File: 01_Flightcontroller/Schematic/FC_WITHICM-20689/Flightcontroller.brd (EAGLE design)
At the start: 63.5 x 63.2 mm, 101 parts, among them Y1 8MHz, Y2 16MHz

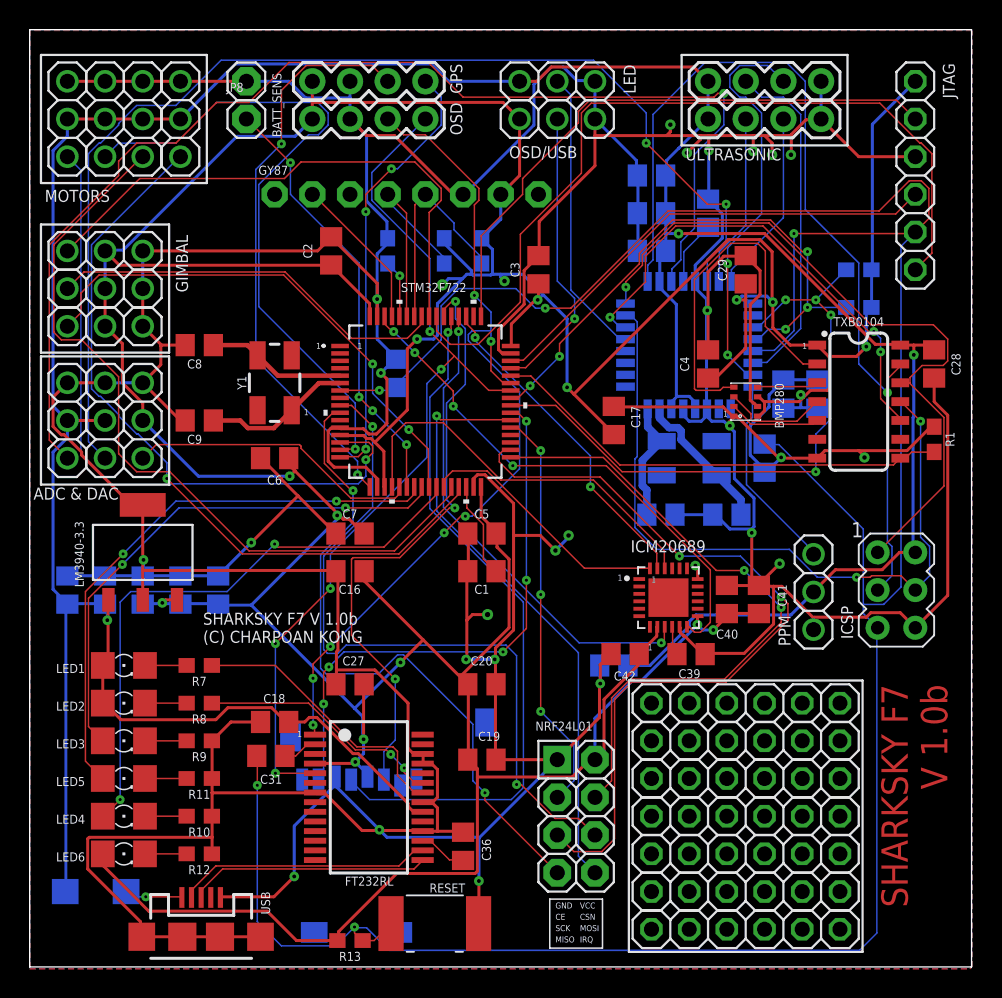
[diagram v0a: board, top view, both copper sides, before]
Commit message: Umdrehen SD Karte
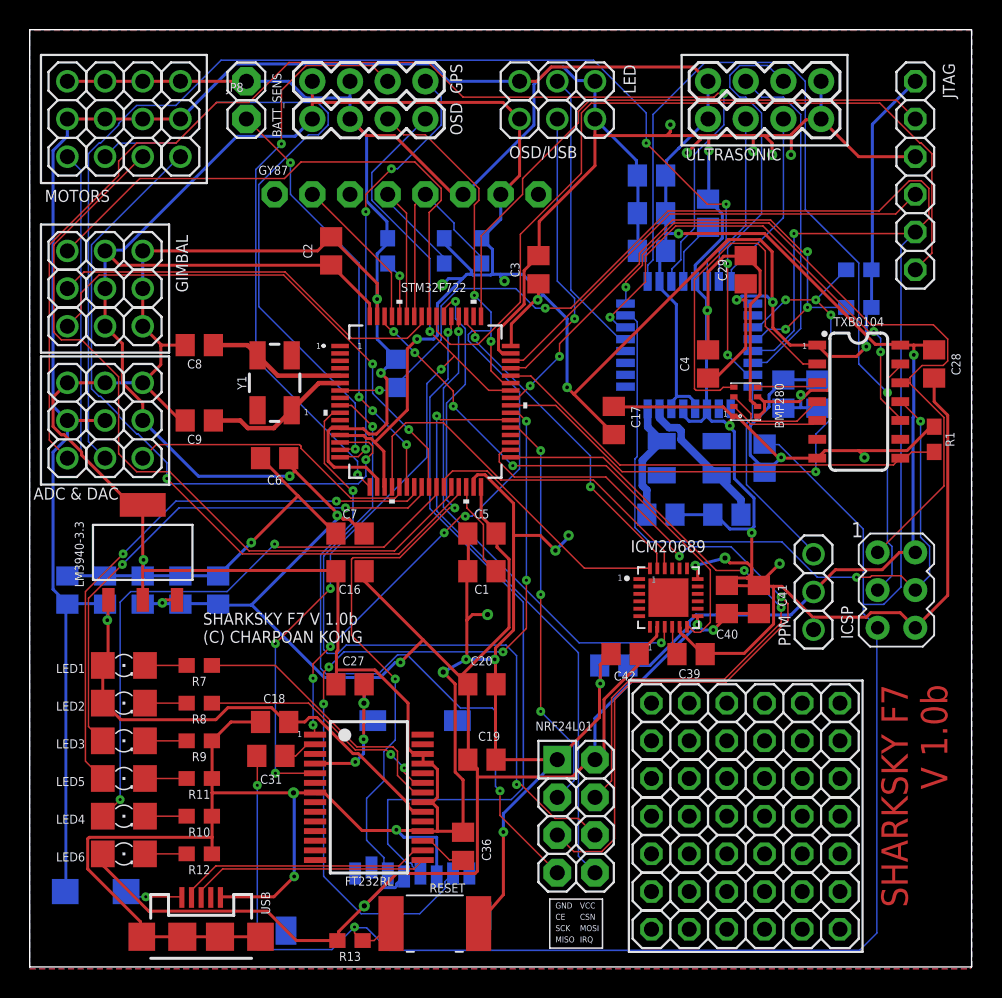
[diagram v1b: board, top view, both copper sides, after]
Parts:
- moved SD_CARD 0.28 mm to (17.5, 48.8), turned to 180 degrees
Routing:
- net SD1_D0: track 37.5 -> 55.1 mm
- net GND: track 558.2 -> 570.2 mm, vias 26 -> 29
- net SD1_CMD: track 41.2 -> 48.6 mm
- net SD1_CK: track 47.5 -> 50.5 mm
- net SPI2_MISO: track 45.0 -> 46.4 mm
- net RST: track 192.7 -> 194.1 mm
- net SPI2_SCLK: track 53.9 -> 54.7 mm
- net VCC: track 371.9 -> 372.1 mm, vias 17 -> 19
